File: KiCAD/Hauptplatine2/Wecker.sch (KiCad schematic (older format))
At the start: 45 parts, among them IC1 ATMEGA328P-P, P1 CONN_5V, P10 LED_Bild2, P11 CONN_MP3, P2 CONN_MP3Player, P3 LED_Bild1, P4 CONN_TASTER, P5 CONN_DREHENCODER, P6 CONN_DISPLAY, P7 CONN_01X02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

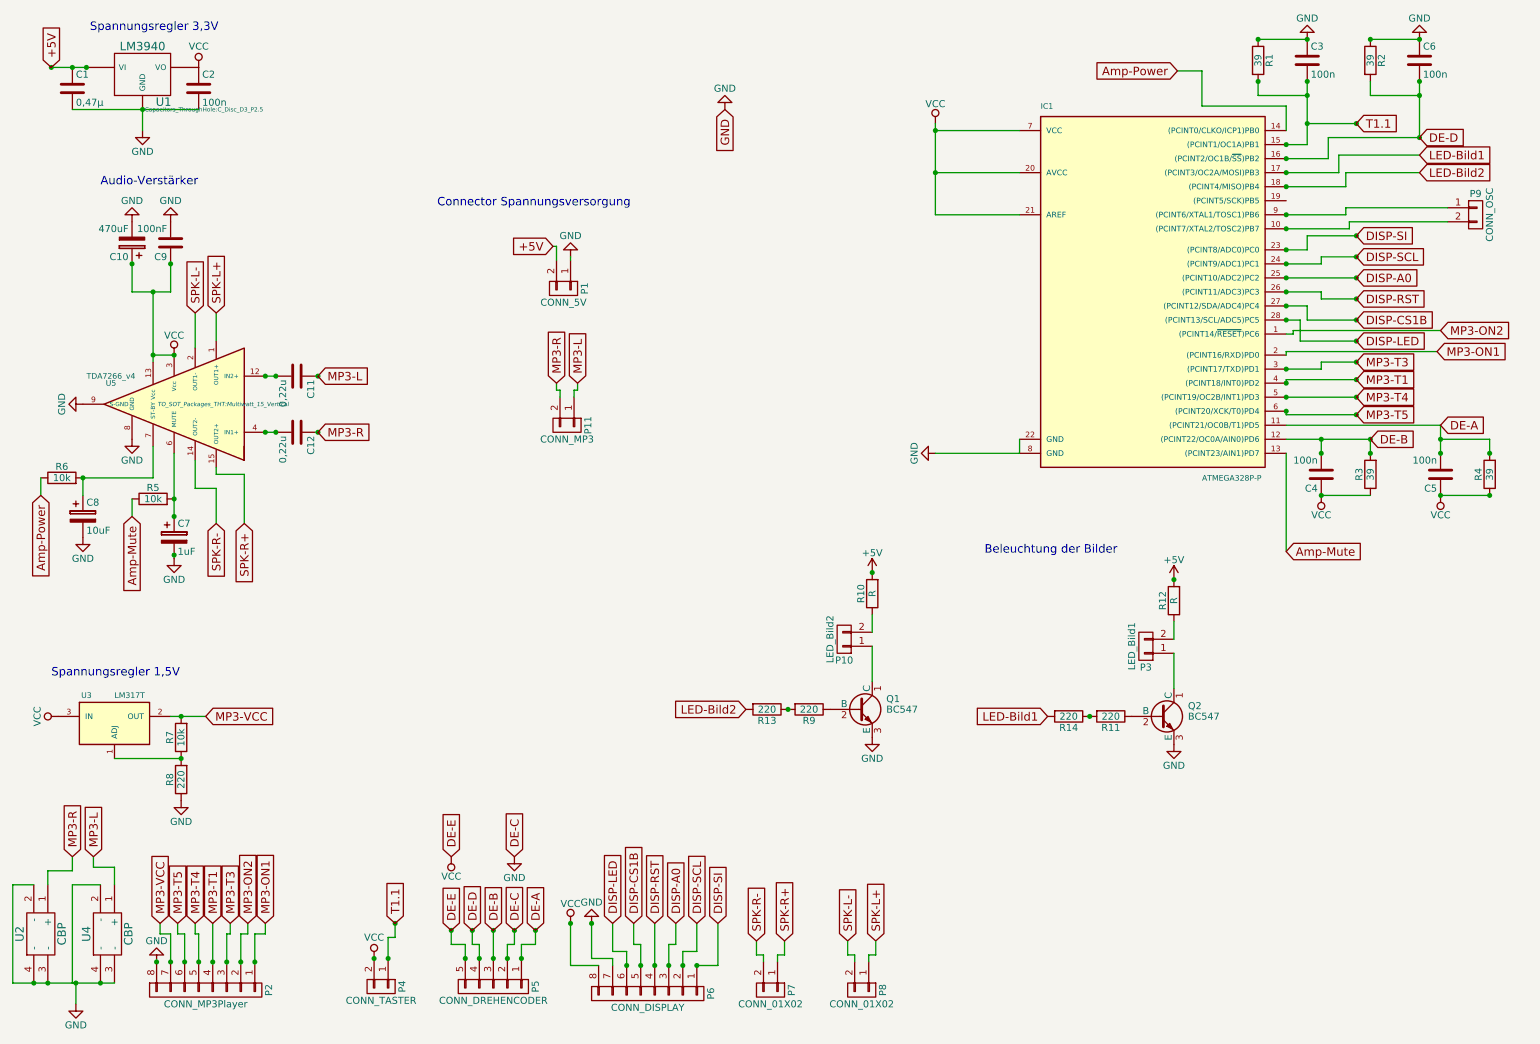
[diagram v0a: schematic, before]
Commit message: PCB enger gepackt. MP3 Player in Code eingebunden.
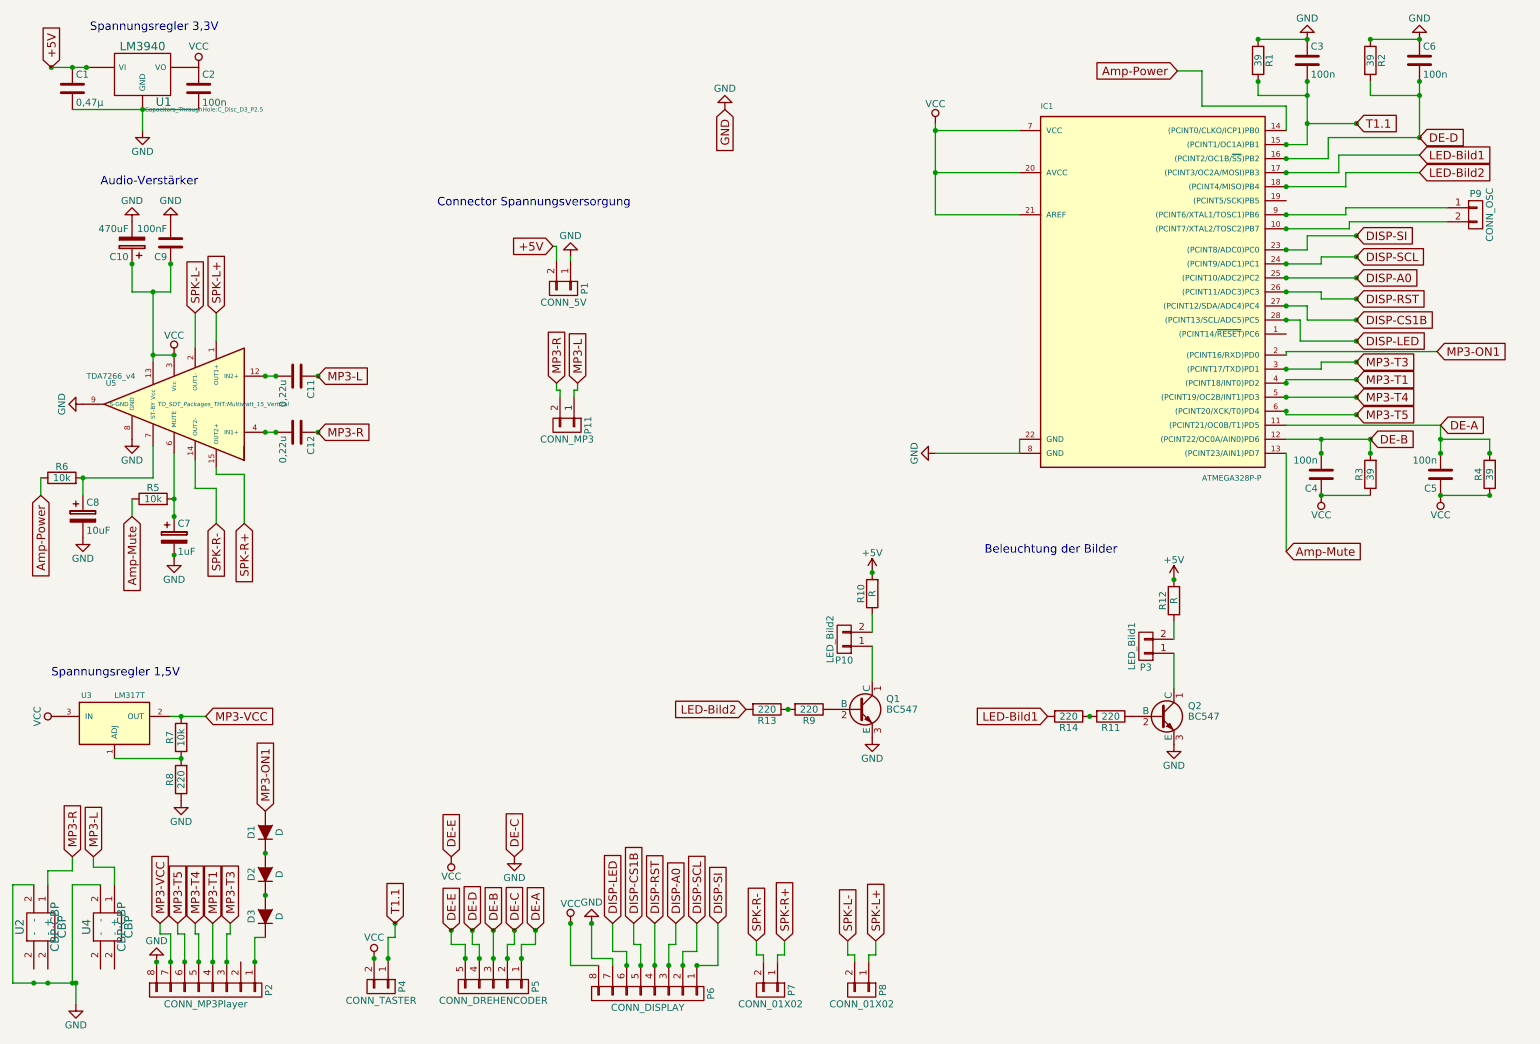
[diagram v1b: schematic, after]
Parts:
- removed U2, U4: CBP, CBP:CBP, symbol CBP-RESCUE-Wecker
- added D1, D2, D3: D, Diodes_ThroughHole:Diode_DO-35_SOD27_Horizontal_RM10, symbol D
- added U2, U4: CBP, CBP:CBP, symbol CBP
- U1: footprint (none) -> Power_Integrations:TO-220
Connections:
- net GND: now also U2.2 (-), U4.2 (-)
- net MP3-L: now also U4.1 (+)
- net MP3-ON1: now also D1.2 (A); no longer P2.1 (P1)
- net MP3-R: now also U2.1 (+)
- net MP3-ON2: no longer names the net of IC1.1 ((PCINT14/~RESET~)PC6)
- net MP3-ON2: no longer P2.2 (P2)
- new net: D3.1 (K), P2.1 (P1)
- new net: D1.1 (K), D2.2 (A)
- new net: D2.1 (K), D3.2 (A)

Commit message: Haupptlatine2 fertig, Masseflächen vergrößert, Leiterbahnen zusammengeschoben
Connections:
- net DE-A: now also P5.2 (P2); no longer P5.1 (P1)
- net GND: now also P5.1 (P1); no longer P5.2 (P2)
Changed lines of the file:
@@
 $EndDescr
 $Comp
-L GND #PWR24
+L GND #PWR01
 U 1 1 5627D0F9
 P 7075 3700
-F 0 "#PWR24" H 7075 3450 50  0001 C CNN
+F 0 "#PWR01" H 7075 3450 50  0001 C CNN
 F 1 "GND" H 7075 3550 50  0000 C CNN
 F 2 "" H 7075 3700 60  0000 C CNN
@@
 $EndComp
 $Comp
-L VCC #PWR23
+L VCC #PWR02
 U 1 1 5627D148
 P 7075 1350
-F 0 "#PWR23" H 7075 1200 50  0001 C CNN
+F 0 "#PWR02" H 7075 1200 50  0001 C CNN
 F 1 "VCC" H 7075 1490 50  0000 C CNN
 F 2 "" H 7075 1350 60  0000 C CNN
@@
 $EndComp
 $Comp
-L VCC #PWR13
+L VCC #PWR03
 U 1 1 5627D2D0
 P 1825 950
-F 0 "#PWR13" H 1825 800 50  0001 C CNN
+F 0 "#PWR03" H 1825 800 50  0001 C CNN
 F 1 "VCC" H 1825 1100 50  0000 C CNN
 F 2 "" H 1825 950 60  0000 C CNN
@@
 $EndComp
 $Comp
-L GND #PWR7
+L GND #PWR04
 U 1 1 5627D2E8
 P 1425 1400
-F 0 "#PWR7" H 1425 1150 50  0001 C CNN
+F 0 "#PWR04" H 1425 1150 50  0001 C CNN
 F 1 "GND" H 1425 1250 50  0000 C CNN
 F 2 "" H 1425 1400 60  0000 C CNN
@@
 Text GLabel 3225 7050 1    60   Input ~ 0
 T1.1
+Text GLabel 4075 7100 1    60   Input ~ 0
+DE-A
 Text GLabel 4225 7100 1    60   Input ~ 0
-DE-A
-Text GLabel 4075 7100 1    60   Input ~ 0
 DE-C
 Text GLabel 3925 7100 1    60   Input ~ 0
@@
 $EndComp
 $Comp
-L GND #PWR27
+L GND #PWR05
 U 1 1 5631658B
 P 9725 750
-F 0 "#PWR27" H 9725 500 50  0001 C CNN
+F 0 "#PWR05" H 9725 500 50  0001 C CNN
 F 1 "GND" H 9725 600 50  0000 C CNN
 F 2 "" H 9725 750 60  0000 C CNN
@@
 $EndComp
 $Comp
-L VCC #PWR14
+L VCC #PWR06
 U 1 1 5631662A
 P 3075 7300
-F 0 "#PWR14" H 3075 7150 50  0001 C CNN
+F 0 "#PWR06" H 3075 7150 50  0001 C CNN
 F 1 "VCC" H 3075 7450 50  0000 C CNN
 F 2 "" H 3075 7300 60  0000 C CNN
@@
 $EndComp
 $Comp
-L GND #PWR29
+L GND #PWR07
 U 1 1 56316E58
 P 10525 750
-F 0 "#PWR29" H 10525 500 50  0001 C CNN
+F 0 "#PWR07" H 10525 500 50  0001 C CNN
 F 1 "GND" H 10525 600 50  0000 C CNN
 F 2 "" H 10525 750 60  0000 C CNN
@@
 SPK-R-
 $Comp
-L GND #PWR3
+L GND #PWR08
 U 1 1 5633D8CB
 P 1000 3350
-F 0 "#PWR3" H 1000 3100 50  0001 C CNN
+F 0 "#PWR08" H 1000 3100 50  0001 C CNN
 F 1 "GND" H 1000 3200 50  0000 C CNN
 F 2 "" H 1000 3350 60  0000 C CNN
@@
 $EndComp
 $Comp
-L GND #PWR11
+L GND #PWR09
 U 1 1 5634F9A3
 P 1650 4450
-F 0 "#PWR11" H 1650 4200 50  0001 C CNN
+F 0 "#PWR09" H 1650 4200 50  0001 C CNN
 F 1 "GND" H 1650 4300 50  0000 C CNN
 F 2 "" H 1650 4450 60  0000 C CNN
@@
 $EndComp
 $Comp
-L GND #PWR4
+L GND #PWR010
 U 1 1 5634FB7C
 P 1000 4300
-F 0 "#PWR4" H 1000 4050 50  0001 C CNN
+F 0 "#PWR010" H 1000 4050 50  0001 C CNN
 F 1 "GND" H 1000 4150 50  0000 C CNN
 F 2 "" H 1000 4300 60  0000 C CNN
@@
 MP3-R
 $Comp
-L GND #PWR8
+L GND #PWR011
 U 1 1 563A5EC8
 P 1525 7325
-F 0 "#PWR8" H 1525 7075 50  0001 C CNN
+F 0 "#PWR011" H 1525 7075 50  0001 C CNN
 F 1 "GND" H 1525 7175 50  0000 C CNN
 F 2 "" H 1525 7325 60  0000 C CNN
@@
 $EndComp
 $Comp
-L VCC #PWR28
+L VCC #PWR012
 U 1 1 56549443
 P 9825 4000
-F 0 "#PWR28" H 9825 3850 50  0001 C CNN
+F 0 "#PWR012" H 9825 3850 50  0001 C CNN
 F 1 "VCC" H 9825 4140 50  0000 C CNN
 F 2 "" H 9825 4000 60  0000 C CNN
@@
 $EndComp
 $Comp
-L VCC #PWR30
+L VCC #PWR013
 U 1 1 5654992D
 P 10675 4000
-F 0 "#PWR30" H 10675 3850 50  0001 C CNN
+F 0 "#PWR013" H 10675 3850 50  0001 C CNN
 F 1 "VCC" H 10675 4140 50  0000 C CNN
 F 2 "" H 10675 4000 60  0000 C CNN
@@
 DE-E
 $Comp
-L VCC #PWR15
+L VCC #PWR014
 U 1 1 5654E6BC
 P 3625 6575
-F 0 "#PWR15" H 3625 6425 50  0001 C CNN
+F 0 "#PWR014" H 3625 6425 50  0001 C CNN
 F 1 "VCC" H 3625 6715 50  0000 C CNN
 F 2 "" H 3625 6575 60  0000 C CNN
@@
 $EndComp
 $Comp
-L GND #PWR16
+L GND #PWR015
 U 1 1 5654E7DF
 P 4075 6575
-F 0 "#PWR16" H 4075 6325 50  0001 C CNN
+F 0 "#PWR015" H 4075 6325 50  0001 C CNN
 F 1 "GND" H 4075 6425 50  0000 C CNN
 F 2 "" H 4075 6575 60  0000 C CNN
@@
 Amp-Power
 $Comp
-L GND #PWR5
+L GND #PWR016
 U 1 1 5657DFBD
 P 1350 2050
-F 0 "#PWR5" H 1350 1800 50  0001 C CNN
+F 0 "#PWR016" H 1350 1800 50  0001 C CNN
 F 1 "GND" H 1350 1900 50  0000 C CNN
 F 2 "" H 1350 2050 60  0000 C CNN
@@
 $EndComp
 $Comp
-L GND #PWR9
+L GND #PWR017
 U 1 1 5657E022
 P 1625 2050
-F 0 "#PWR9" H 1625 1800 50  0001 C CNN
+F 0 "#PWR017" H 1625 1800 50  0001 C CNN
 F 1 "GND" H 1625 1900 50  0000 C CNN
 F 2 "" H 1625 2050 60  0000 C CNN
@@
 $EndComp
 $Comp
-L VCC #PWR10
+L VCC #PWR018
 U 1 1 5657E6F9
 P 1650 3000
-F 0 "#PWR10" H 1650 2850 50  0001 C CNN
+F 0 "#PWR018" H 1650 2850 50  0001 C CNN
 F 1 "VCC" H 1650 3140 50  0000 C CNN
 F 2 "" H 1650 3000 60  0000 C CNN
@@
 Spannungsregler 1,5V
 $Comp
-L VCC #PWR1
+L VCC #PWR019
 U 1 1 56577A6D
 P 825 5575
-F 0 "#PWR1" H 825 5425 50  0001 C CNN
+F 0 "#PWR019" H 825 5425 50  0001 C CNN
 F 1 "VCC" H 825 5725 50  0000 C CNN
 F 2 "" H 825 5575 60  0000 C CNN
@@
 $EndComp
 $Comp
-L GND #PWR12
+L GND #PWR020
 U 1 1 56578070
 P 1700 6175
-F 0 "#PWR12" H 1700 5925 50  0001 C CNN
+F 0 "#PWR020" H 1700 5925 50  0001 C CNN
 F 1 "GND" H 1700 6025 50  0000 C CNN
 F 2 "" H 1700 6175 60  0000 C CNN
@@
 Connection ~ 1700 5575
 $Comp
-L GND #PWR2
+L GND #PWR021
 U 1 1 565876AB
 P 950 7625
-F 0 "#PWR2" H 950 7375 50  0001 C CNN
+F 0 "#PWR021" H 950 7375 50  0001 C CNN
 F 1 "GND" H 950 7475 50  0000 C CNN
 F 2 "" H 950 7625 60  0000 C CNN
@@
 	500  6775 500  7475
 Wire Wire Line
-	500  7475 950  7475
+	500  7475 1225 7475
 Connection ~ 650  7475
 Wire Wire Line
@@
 Connection ~ 1500 2550
 $Comp
-L GND #PWR6
+L GND #PWR022
 U 1 1 5658A1B2
 P 1350 3600
-F 0 "#PWR6" H 1350 3350 50  0001 C CNN
+F 0 "#PWR022" H 1350 3350 50  0001 C CNN
 F 1 "GND" H 1350 3450 50  0000 C CNN
 F 2 "" H 1350 3600 60  0000 C CNN
@@
 LED-Bild1
 $Comp
-L +5V #PWR25
+L +5V #PWR023
 U 1 1 5658E08E
 P 8775 4600
-F 0 "#PWR25" H 8775 4450 50  0001 C CNN
+F 0 "#PWR023" H 8775 4450 50  0001 C CNN
 F 1 "+5V" H 8775 4740 50  0000 C CNN
 F 2 "" H 8775 4600 60  0000 C CNN
@@
 	8775 5125 8775 5375
 $Comp
-L GND #PWR26
+L GND #PWR024
 U 1 1 5658EC2F
 P 8775 5775
-F 0 "#PWR26" H 8775 5525 50  0001 C CNN
+F 0 "#PWR024" H 8775 5525 50  0001 C CNN
 F 1 "GND" H 8775 5625 50  0000 C CNN
 F 2 "" H 8775 5775 60  0000 C CNN
@@
 LED-Bild2
 $Comp
-L +5V #PWR21
+L +5V #PWR025
 U 1 1 5658FE82
 P 6625 4550
-F 0 "#PWR21" H 6625 4400 50  0001 C CNN
+F 0 "#PWR025" H 6625 4400 50  0001 C CNN
 F 1 "+5V" H 6625 4690 50  0000 C CNN
 F 2 "" H 6625 4550 60  0000 C CNN
@@
 	6625 5075 6625 5325
 $Comp
-L GND #PWR22
+L GND #PWR026
 U 1 1 5658FE90
 P 6625 5725
-F 0 "#PWR22" H 6625 5475 50  0001 C CNN
+F 0 "#PWR026" H 6625 5475 50  0001 C CNN
 F 1 "GND" H 6625 5575 50  0000 C CNN
 F 2 "" H 6625 5725 60  0000 C CNN
@@
 	4625 7300 4625 7050
 $Comp
-L VCC #PWR18
+L VCC #PWR027
 U 1 1 5658A7BA
 P 4475 7050
-F 0 "#PWR18" H 4475 6900 50  0001 C CNN
+F 0 "#PWR027" H 4475 6900 50  0001 C CNN
 F 1 "VCC" H 4475 7190 50  0000 C CNN
 F 2 "" H 4475 7050 60  0000 C CNN
@@
 $EndComp
 $Comp
-L GND #PWR19
+L GND #PWR028
 U 1 1 5658A869
 P 4625 7050
-F 0 "#PWR19" H 4625 6800 50  0001 C CNN
+F 0 "#PWR028" H 4625 6800 50  0001 C CNN
 F 1 "GND" H 4625 6900 50  0000 C CNN
 F 2 "" H 4625 7050 60  0000 C CNN
@@
 $EndComp
 $Comp
-L GND #PWR17
+L GND #PWR029
 U 1 1 5658A552
 P 4475 2300
-F 0 "#PWR17" H 4475 2050 50  0001 C CNN
+F 0 "#PWR029" H 4475 2050 50  0001 C CNN
 F 1 "GND" H 4475 2150 50  0000 C CNN
 F 2 "" H 4475 2300 60  0000 C CNN
@@
 $EndComp
 $Comp
-L GND #PWR20
+L GND #PWR030
 U 1 1 565935BC
 P 5575 1250
-F 0 "#PWR20" H 5575 1000 50  0001 C CNN
+F 0 "#PWR030" H 5575 1000 50  0001 C CNN
 F 1 "GND" H 5575 1100 50  0000 C CNN
 F 2 "" H 5575 1250 60  0000 C CNN
@@
 	0    -1   -1   0
 $EndComp
+Wire Wire Line
+	650  7375 650  7475
+Wire Wire Line
+	750  7375 750  7475
+Wire Wire Line
+	1125 7475 1125 7375
+Wire Wire Line
+	1225 7475 1225 7375
+Connection ~ 1125 7475
 $EndSCHEMATC

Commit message: Beleuchtung Plexiglas1 hinzugefügt
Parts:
- C2: value 100n -> 47u; symbol C -> CP
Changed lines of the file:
@@
 $EndComp
 $Comp
-L C C2
+L CP C2
 U 1 1 5658AA18
 P 1825 1100
 F 0 "C2" H 1850 1200 50  0000 L CNN
-F 1 "100n" H 1850 1000 50  0000 L CNN
+F 1 "47u" H 1850 1000 50  0000 L CNN
 F 2 "Capacitors_ThroughHole:C_Disc_D3_P2.5" H 1863 950 30  0000 C CNN
 F 3 "" H 1825 1100 60  0000 C CNN
